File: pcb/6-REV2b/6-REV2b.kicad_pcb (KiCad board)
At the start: 4 copper layers, 80 x 80.2 mm, 227 parts, among them J201 Conn_01x03, J202 TYPE-C-31-M-12, J301 Conn_01x10, J302 Conn_01x09, Q202 MMBT7002K, Q300 SI2301, Q301 SI2301, Q302 SI2301, Q303 SI2301, Q304 SI2301, Q305 SI2301, Q306 SI2301, Q307 SI2301, Q401 BCM857, Q402 SI2301, Q601 MMDT3906, Q602 SI2301, SW101 SW_SPST, SW102 4P_button_sw, U102 W25Q128JVSIQ, U105 MT29F1G01ABAFDWB, U2 74LVC8T245BQ, U3 TLV74311PDBVR, U301 AiP74LVC1T45GC363.TR, U302 AiP74LVC1T45GC363.TR, U303 AiP74LVC1T45GC363.TR, U304 AiP74LVC1T45GC363.TR, U305 AiP74LVC1T45GC363.TR, U306 AiP74LVC1T45GC363.TR, U307 AiP74LVC1T45GC363.TR, U308 AiP74LVC1T45GC363.TR, U401 ME6211A33PG-N, U402 CD4067, U403 AP2127, U404 LMV321, U503 74HCT245BQ, U504 LMV324, U505 LMV324, U506 LMV321, U601 LMV321A, U602 LMV331, U603 LMV321, Y101 12Mhz

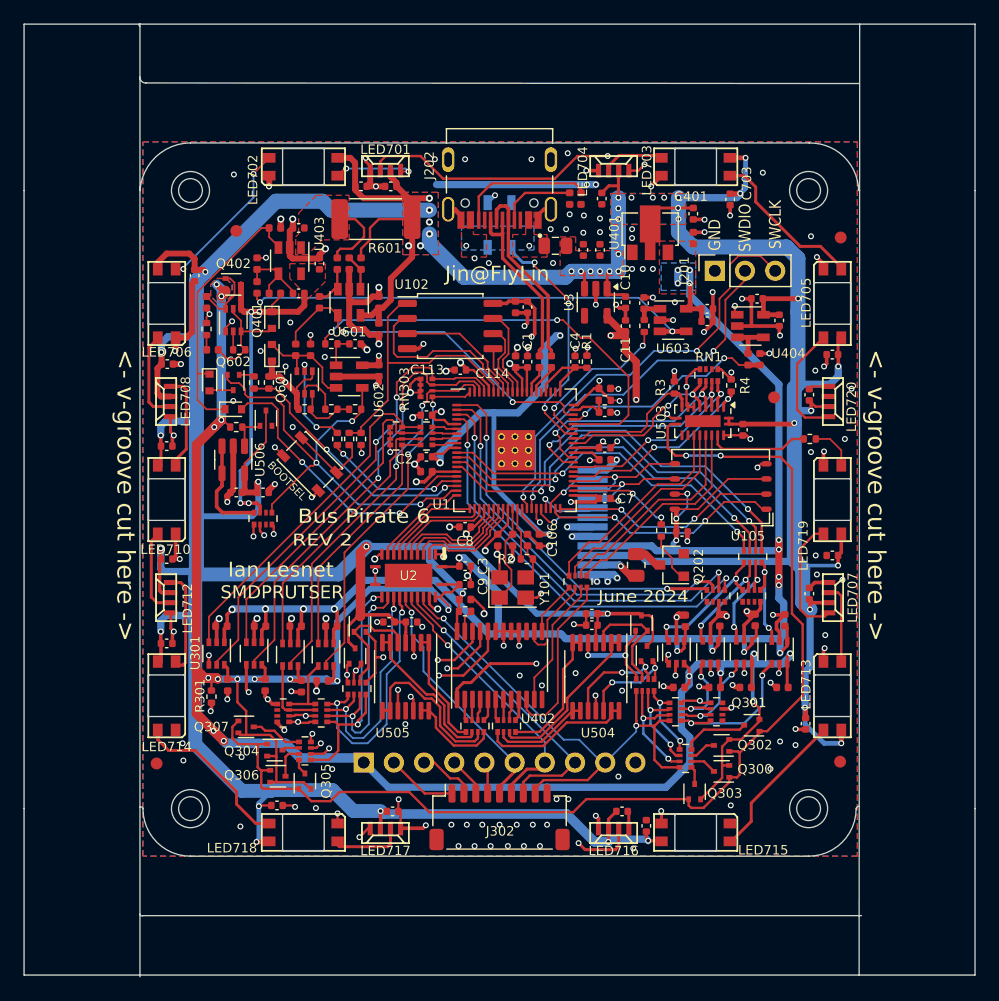
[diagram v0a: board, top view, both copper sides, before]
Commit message: 3d models on BP 6 pcb
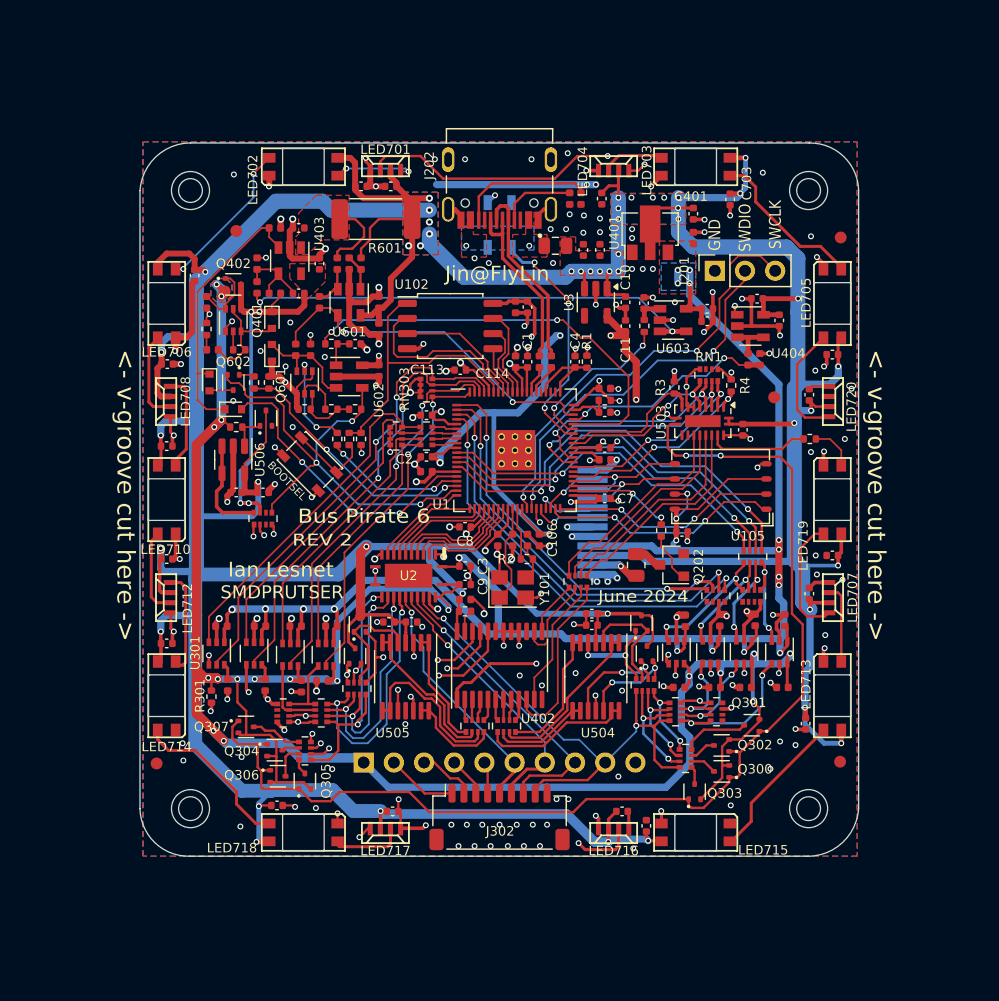
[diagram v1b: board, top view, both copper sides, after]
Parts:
- D500, D501, D502, D503, D504, Q300, Q301, Q302, Q303, Q304, Q305, Q306, Q307, Q402, Q602: footprint Package_TO_SOT_SMD:SOT-523 -> library:SOT-523
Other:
- board size 80 x 80.2 mm -> 60.5 x 60 mm
